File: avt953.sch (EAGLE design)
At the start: 10 parts, among them IC1 AT24CP, IC4 MAX232ECWE, X1 RJ45-6L2-B, X2 MKDS_5/3-7,62

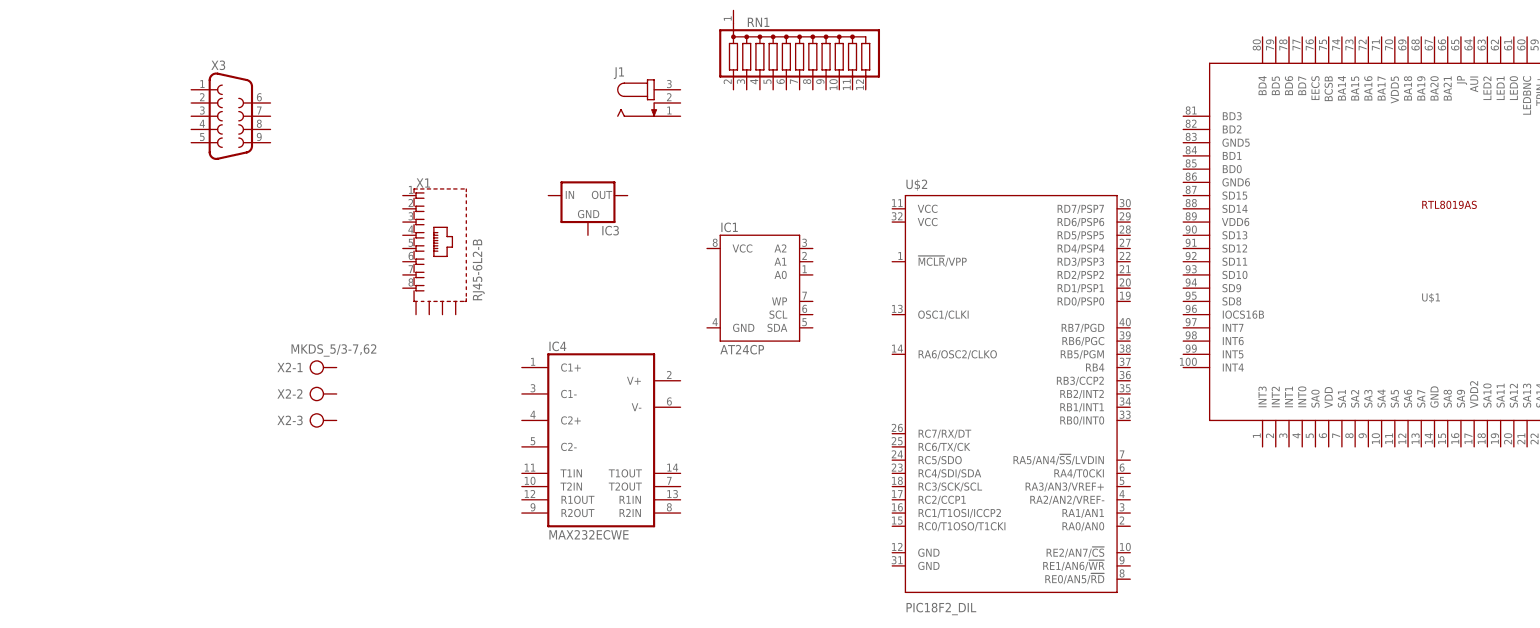
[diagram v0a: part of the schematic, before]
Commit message: Dopasowano nazwy na schemacie do wytycznych.
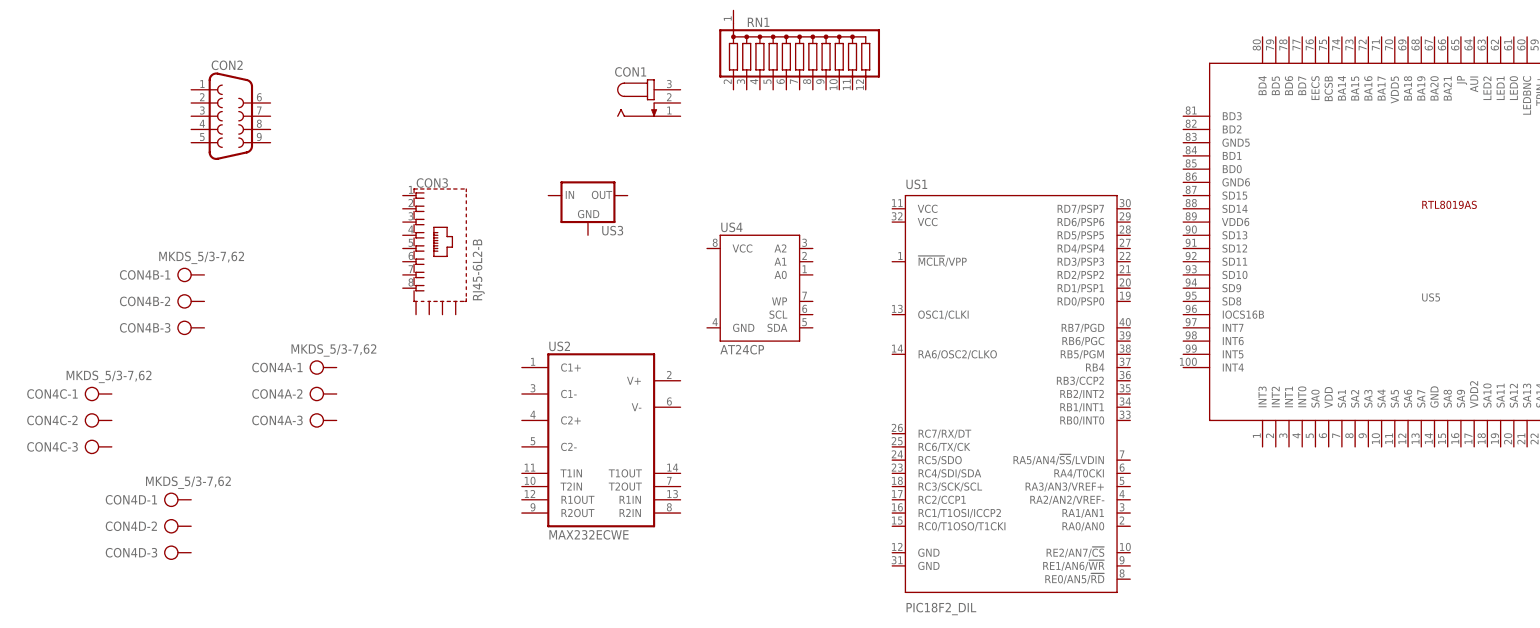
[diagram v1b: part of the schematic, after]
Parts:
- added CON4B, CON4C, CON4D: MKDS_5/3-7,62, con-phoenix-mkds_5:MKDS_5/3-7,62
- renumbered IC1 to US4, IC3 to US3, IC4 to US2, J1 to CON1, U$1 to US5, U$2 to US1, X1 to CON3, X2 to CON4A, X3 to CON2
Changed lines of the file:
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@@
 </classes>
 <parts>
-<part name="X1" library="con-tycoelectronics" deviceset="RJ45*2" device="-B" technology="-6L"/>
-<part name="IC1" library="atmel" deviceset="AT24C*" device="P"/>
-<part name="U$1" library="rtl8019as" deviceset="RTL8019AS" device=""/>
-<part name="IC3" library="v-reg" deviceset="78XXL" device=""/>
-<part name="J1" library="con-jack" deviceset="JACK-PLUG" device="0"/>
-<part name="X2" library="con-phoenix-mkds_5" deviceset="MKDS_5/3-" device="7,62"/>
-<part name="X3" library="con-subd" deviceset="F09" device="HP"/>
-<part name="IC4" library="maxim" deviceset="MAX232ECWE" device=""/>
+<part name="CON3" library="con-tycoelectronics" deviceset="RJ45*2" device="-B" technology="-6L"/>
+<part name="US4" library="atmel" deviceset="AT24C*" device="P"/>
+<part name="US5" library="rtl8019as" deviceset="RTL8019AS" device=""/>
+<part name="US3" library="v-reg" deviceset="78XXL" device=""/>
+<part name="CON1" library="con-jack" deviceset="JACK-PLUG" device="0"/>
+<part name="CON4A" library="con-phoenix-mkds_5" deviceset="MKDS_5/3-" device="7,62"/>
+<part name="CON2" library="con-subd" deviceset="F09" device="HP"/>
+<part name="US2" library="maxim" deviceset="MAX232ECWE" device=""/>
 <part name="RN1" library="resistor-sil" deviceset="G11R" device=""/>
-<part name="U$2" library="microchip-custom" deviceset="PIC18F*2_DIL" device=""/>
+<part name="US1" library="microchip-custom" deviceset="PIC18F*2_DIL" device=""/>
+<part name="CON4B" library="con-phoenix-mkds_5" deviceset="MKDS_5/3-" device="7,62"/>
+<part name="CON4C" library="con-phoenix-mkds_5" deviceset="MKDS_5/3-" device="7,62"/>
+<part name="CON4D" library="con-phoenix-mkds_5" deviceset="MKDS_5/3-" device="7,62"/>
 </parts>
 <sheets>
@@
 </plain>
 <instances>
-<instance part="X1" gate="G$1" x="40.64" y="50.8"/>
-<instance part="IC1" gate="G$1" x="101.6" y="43.18"/>
-<instance part="U$1" gate="G$1" x="233.68" y="50.8"/>
-<instance part="IC3" gate="A" x="68.58" y="60.96"/>
-<instance part="J1" gate="G$1" x="81.28" y="78.74"/>
-<instance part="X2" gate="-1" x="15.24" y="27.94"/>
-<instance part="X2" gate="-2" x="15.24" y="22.86"/>
-<instance part="X2" gate="-3" x="15.24" y="17.78"/>
-<instance part="X3" gate="G$1" x="0" y="76.2"/>
-<instance part="IC4" gate="G$1" x="71.12" y="15.24"/>
+<instance part="CON3" gate="G$1" x="40.64" y="50.8"/>
+<instance part="US4" gate="G$1" x="101.6" y="43.18"/>
+<instance part="US5" gate="G$1" x="233.68" y="50.8"/>
+<instance part="US3" gate="A" x="68.58" y="60.96"/>
+<instance part="CON1" gate="G$1" x="81.28" y="78.74"/>
+<instance part="CON4A" gate="-1" x="15.24" y="27.94"/>
+<instance part="CON4A" gate="-2" x="15.24" y="22.86"/>
+<instance part="CON4A" gate="-3" x="15.24" y="17.78"/>
+<instance part="CON2" gate="G$1" x="0" y="76.2"/>
+<instance part="US2" gate="G$1" x="71.12" y="15.24"/>
 <instance part="RN1" gate="A" x="109.22" y="86.36"/>
-<instance part="U$2" gate="G$1" x="149.86" y="22.86"/>
+<instance part="US1" gate="G$1" x="149.86" y="22.86"/>
+<instance part="CON4B" gate="-1" x="-10.16" y="45.72"/>
+<instance part="CON4B" gate="-2" x="-10.16" y="40.64"/>
+<instance part="CON4B" gate="-3" x="-10.16" y="35.56"/>
+<instance part="CON4C" gate="-1" x="-27.94" y="22.86"/>
+<instance part="CON4C" gate="-2" x="-27.94" y="17.78"/>
+<instance part="CON4C" gate="-3" x="-27.94" y="12.7"/>
+<instance part="CON4D" gate="-1" x="-12.7" y="2.54"/>
+<instance part="CON4D" gate="-2" x="-12.7" y="-2.54"/>
+<instance part="CON4D" gate="-3" x="-12.7" y="-7.62"/>
 </instances>
 <busses>

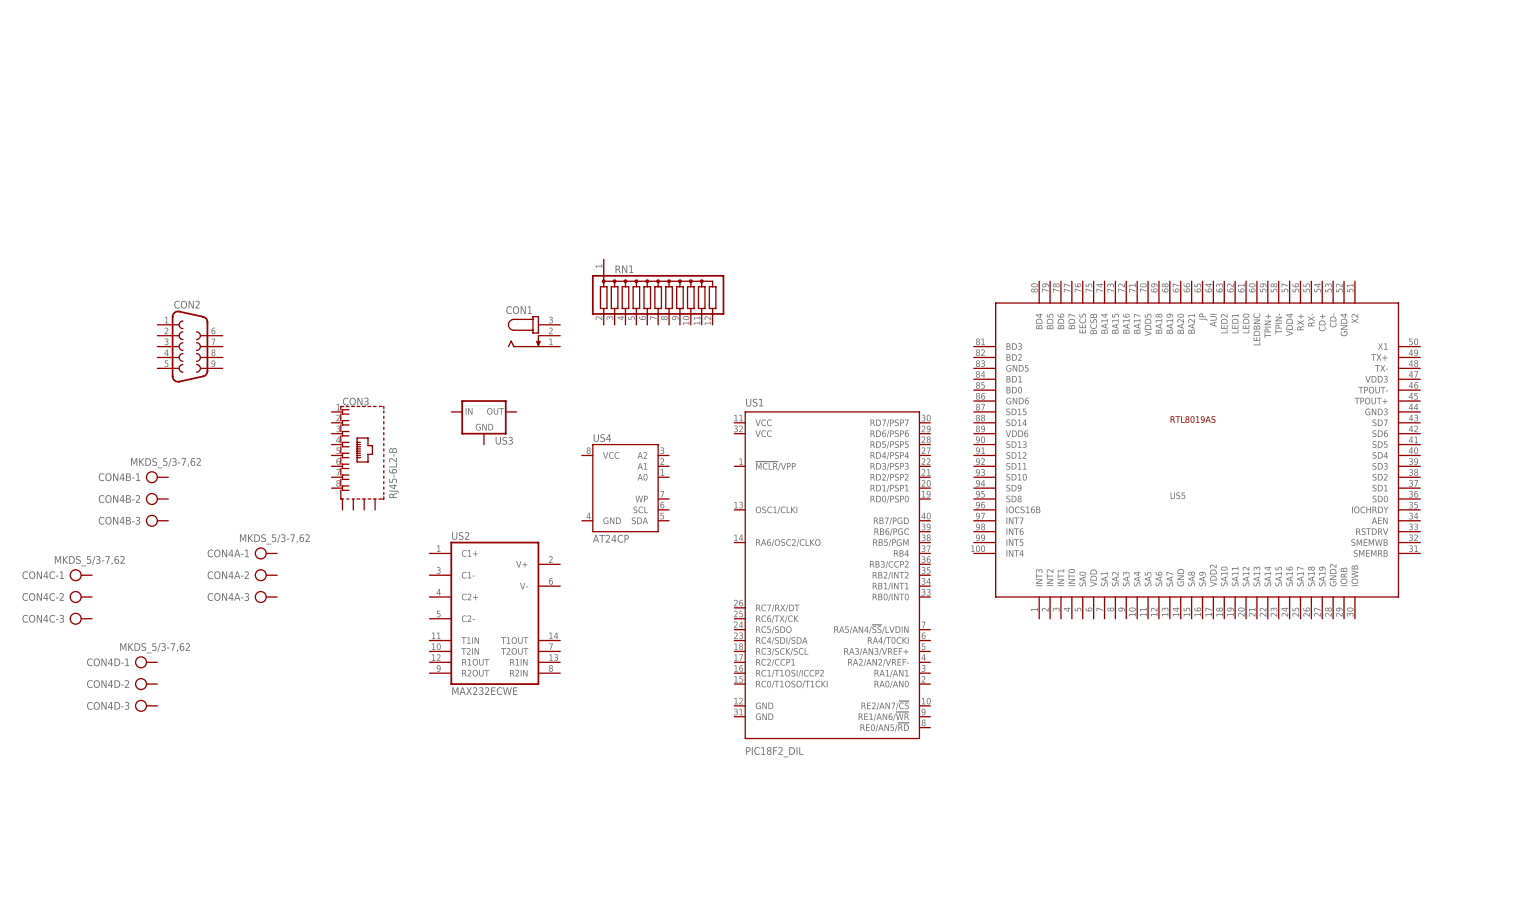
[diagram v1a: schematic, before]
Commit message: Dodano bibliotekę z transformatorem ethernetowym 10BASE-T YCL-20F001N. Umieszczono to trafo na schemacie.
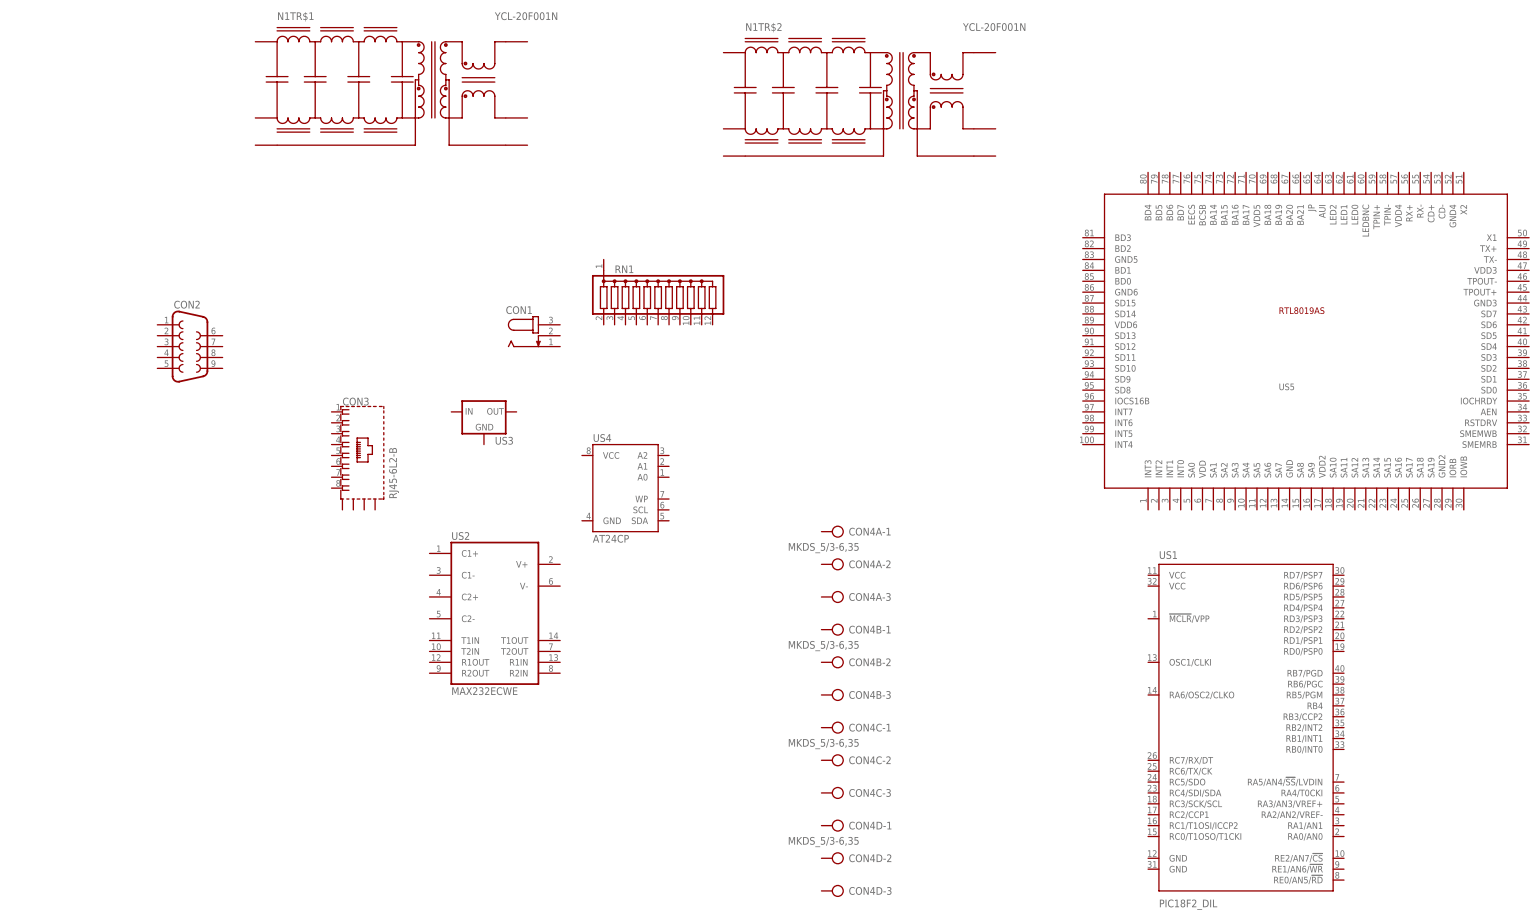
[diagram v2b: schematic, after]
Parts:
- added N1: YCL-20F001N, trafo:YCL-20F001N
- CON4A, CON4B, CON4C, CON4D: value MKDS_5/3-7,62 -> MKDS_5/3-6,35; device con-phoenix-mkds_5:MKDS_5/3-7,62 -> con-phoenix-mkds_5:MKDS_5/3-6,35
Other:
- moved on the sheet: CON4A-1, CON4A-2, CON4A-3, CON4B-1, CON4B-2, CON4B-3, CON4C-1, CON4C-2, CON4C-3, CON4D-1, CON4D-2, CON4D-3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
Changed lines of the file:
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@@
 <part name="US3" library="v-reg" deviceset="78XXL" device=""/>
 <part name="CON1" library="con-jack" deviceset="JACK-PLUG" device="0"/>
-<part name="CON4A" library="con-phoenix-mkds_5" deviceset="MKDS_5/3-" device="7,62"/>
+<part name="CON4A" library="con-phoenix-mkds_5" deviceset="MKDS_5/3-" device="6,35" value="MKDS_5/3-6,35"/>
 <part name="CON2" library="con-subd" deviceset="F09" device="HP"/>
 <part name="US2" library="maxim" deviceset="MAX232ECWE" device=""/>
 <part name="RN1" library="resistor-sil" deviceset="G11R" device=""/>
 <part name="US1" library="microchip-custom" deviceset="PIC18F*2_DIL" device=""/>
-<part name="CON4B" library="con-phoenix-mkds_5" deviceset="MKDS_5/3-" device="7,62"/>
-<part name="CON4C" library="con-phoenix-mkds_5" deviceset="MKDS_5/3-" device="7,62"/>
-<part name="CON4D" library="con-phoenix-mkds_5" deviceset="MKDS_5/3-" device="7,62"/>
+<part name="CON4B" library="con-phoenix-mkds_5" deviceset="MKDS_5/3-" device="6,35" value="MKDS_5/3-6,35"/>
+<part name="CON4C" library="con-phoenix-mkds_5" deviceset="MKDS_5/3-" device="6,35" value="MKDS_5/3-6,35"/>
+<part name="CON4D" library="con-phoenix-mkds_5" deviceset="MKDS_5/3-" device="6,35" value="MKDS_5/3-6,35"/>
+<part name="N1" library="trafo" deviceset="YCL-20F001?" device="N"/>
 </parts>
 <sheets>
@@
 <instance part="CON3" gate="G$1" x="40.64" y="50.8"/>
 <instance part="US4" gate="G$1" x="101.6" y="43.18"/>
-<instance part="US5" gate="G$1" x="233.68" y="50.8"/>
+<instance part="US5" gate="G$1" x="259.08" y="76.2"/>
 <instance part="US3" gate="A" x="68.58" y="60.96"/>
 <instance part="CON1" gate="G$1" x="81.28" y="78.74"/>
-<instance part="CON4A" gate="-1" x="15.24" y="27.94"/>
-<instance part="CON4A" gate="-2" x="15.24" y="22.86"/>
-<instance part="CON4A" gate="-3" x="15.24" y="17.78"/>
+<instance part="CON4A" gate="-1" x="152.4" y="33.02" rot="R180"/>
+<instance part="CON4A" gate="-2" x="152.4" y="25.4" rot="R180"/>
+<instance part="CON4A" gate="-3" x="152.4" y="17.78" rot="R180"/>
 <instance part="CON2" gate="G$1" x="0" y="76.2"/>
 <instance part="US2" gate="G$1" x="71.12" y="15.24"/>
 <instance part="RN1" gate="A" x="109.22" y="86.36"/>
-<instance part="US1" gate="G$1" x="149.86" y="22.86"/>
-<instance part="CON4B" gate="-1" x="-10.16" y="45.72"/>
-<instance part="CON4B" gate="-2" x="-10.16" y="40.64"/>
-<instance part="CON4B" gate="-3" x="-10.16" y="35.56"/>
-<instance part="CON4C" gate="-1" x="-27.94" y="22.86"/>
-<instance part="CON4C" gate="-2" x="-27.94" y="17.78"/>
-<instance part="CON4C" gate="-3" x="-27.94" y="12.7"/>
-<instance part="CON4D" gate="-1" x="-12.7" y="2.54"/>
-<instance part="CON4D" gate="-2" x="-12.7" y="-2.54"/>
-<instance part="CON4D" gate="-3" x="-12.7" y="-7.62"/>
+<instance part="US1" gate="G$1" x="246.38" y="-12.7"/>
+<instance part="CON4B" gate="-1" x="152.4" y="10.16" rot="R180"/>
+<instance part="CON4B" gate="-2" x="152.4" y="2.54" rot="R180"/>
+<instance part="CON4B" gate="-3" x="152.4" y="-5.08" rot="R180"/>
+<instance part="CON4C" gate="-1" x="152.4" y="-12.7" rot="R180"/>
+<instance part="CON4C" gate="-2" x="152.4" y="-20.32" rot="R180"/>
+<instance part="CON4C" gate="-3" x="152.4" y="-27.94" rot="R180"/>
+<instance part="CON4D" gate="-1" x="152.4" y="-35.56" rot="R180"/>
+<instance part="CON4D" gate="-2" x="152.4" y="-43.18" rot="R180"/>
+<instance part="CON4D" gate="-3" x="152.4" y="-50.8" rot="R180"/>
+<instance part="N1" gate="TR$1" x="40.64" y="149.86"/>
+<instance part="N1" gate="TR$2" x="149.86" y="147.32"/>
 </instances>
 <busses>

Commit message: Zaprojektowano kompletny schemat układu.Przygotowano na jego podstawie pusty projekt płytki PCB i rozmieszczono co większe elementy.
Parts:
- removed RN1: (no value), resistor-sil:G11R
- added C1: 100u, resistor:CPOL-EUE5-13
- added C10, C11, C12, C2, C8, C9: 100n, resistor:C-EUC1206K
- added C13, C14, C15, C16, C17, C18, C21, C6, C7: 100N, resistor:C-EUC1206K
- added C19, C20: 100n,400V, resistor:C-EU075-032X103
- added C3: 220u, resistor:CPOL-EUE5-13
- added C4, C5: 15p, resistor:C-EUC1206K
- added D1: 1N4147, diode:1N4148DO35-10
- added D2: SYSTEM, led:LED5MM
- added D3, D5: LL4148, diode:CGRM4001-G
- added LED: TX_RX, led:LED5MM
- added R13: 11x10k, resistor-sil:G11R
- added R2, R9: 330, resistor:R-EU_M3216
- added R3: 10K, resistor:R-EU_M3216
- added R4, R5: 4K7, resistor:R-EU_M3216
- added R6: 20K, resistor:R-EU_M3216
- added R7: 200, resistor:R-EU_M3216
- added R8: 22K, resistor:R-EU_M3216
- added S: (no value), switch-omron:10-XX
- added X1, X2: 20MHz, crystal:CRYSTALHC49S
- US2: value MAX232ECWE -> MAX232A
- US3: value (none) -> 78L08
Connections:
- new net A0: US1.RB0/INT0, US5.SA0
- new net A1: US1.RB1/INT1, US5.SA1
- new net A2: US1.RB2/INT2, US5.SA2
- new net A3: US1.RB3/CCP2, US5.SA3
- new net A4: US1.RB4, US5.SA4
- new net GND: C1.-, C11.2, C12.2, C13.1, C14.2, C15.2, C16.1, C17.2, C18.2, C19.2, C2.2, C20.2, C21.2, C3.-, C4.2, C5.2, C6.2, C7.2, CON1.1, CON1.2, CON3.S@1, CON3.S@2, CON3.S@3, CON3.S@4, CON4D-3.KL, LED.C, R8.1, S.S, S.S1, US1.GND, US1.GND@1, US2G$1.T2IN, US3.GND, US4.A0, US4.A1, US4.A2, US4.GND, US4.WP, US5.AEN, US5.AUI, US5.GND, US5.GND2, US5.GND3, US5.GND4, US5.GND5, US5.GND6, US5.SA10, US5.SA11, US5.SA12, US5.SA13, US5.SA14, US5.SA15, US5.SA16, US5.SA17, US5.SA18, US5.SA19, US5.SA5, US5.SA6, US5.SA7
- new net IN0: CON4A-1.KL, R13.12, US1.RA0/AN0
- new net IN1: CON4A-2.KL, R13.11, US1.RA1/AN1
- new net IN10: CON4D-2.KL, R13.2, US1.RC5/SDO
- new net IN2: CON4A-3.KL, R13.10, US1.RA2/AN2/VREF-
- new net IN3: CON4B-1.KL, R13.9, US1.RA3/AN3/VREF+
- new net IN4: CON4B-2.KL, R13.8, US1.RA5/AN4/!SS!/LVDIN
- new net IN5: CON4B-3.KL, R13.7, US1.RB6/PGC
- new net IN6: CON4C-1.KL, R13.6, US1.RB7/PGD
- new net IN7: CON4C-2.KL, R13.5, US1.RC0/T1OSO/T1CKI
- new net IN8: CON4C-3.KL, R13.4, US1.RC1/T1OSI/ICCP2
- new net IN9: CON4D-1.KL, R13.3, US1.RC2/CCP1
- new net IOR: US1.RE0/AN5/!RD, US5.IORB
- new net IOW: US1.RE1/AN6/!WR, US5.IOWB
- new net N$1: C9.2, US2G$1.V+
- new net N$10: CON2.7, US2G$1.R2IN
- new net N$11: CON1.3, D1.A
- new net N$12: C1.+, D1.C, US3.IN
- new net N$13: CON3.1, N1TR$1.P$4
- new net N$14: CON3.2, N1TR$1.P$6
- new net N$15: CON3.3, N1TR$2.P$4
- new net N$16: CON3.6, N1TR$2.P$6
- new net N$17: C19.1, N1TR$1.P$5
- new net N$18: C20.1, N1TR$2.P$5
- new net N$19: C18.1, N1TR$2.P$2
- new net N$2: C12.1, US2G$1.V-
- new net N$20: C17.1, N1TR$1.P$2
- new net N$21: N1TR$1.P$3, US5.TPOUT+
- new net N$22: N1TR$2.P$3, R7.1, US5.TPIN+
- new net N$23: N1TR$1.P$1, US5.TPOUT-
- new net N$24: US5.X1, X2.2
- new net N$25: N1TR$2.P$1, R7.2, US5.TPIN-
- new net N$26: D3.A, US5.LED1
- new net N$27: R8.2, US5.IOCS16B
- new net N$28: US5.X2, X2.1
- new net N$29: D5.A, US5.LED2
- new net N$3: C10.2, US2G$1.C1-
- new net N$30: D3.C, D5.C, R9.2
- new net N$31: LED.A, R9.1
- new net N$32: C5.1, US1.OSC1/CLKI, X1.1
- new net N$33: C4.1, US1.RA6/OSC2/CLKO, X1.2
- new net N$34: R4.2, US1.RC4/SDI/SDA, US4.SDA
- new net N$35: R3.1, US1.!MCLR!/VPP
- new net N$36: R2.2, US1.RA4/T0CKI
- new net N$37: R5.2, US1.RC3/SCK/SCL, US4.SCL
- new net N$38: D2.C, R2.1
- new net N$4: C10.1, US2G$1.C1+
- new net N$40: S.P, S.P1, US1.RB5/PGM
- new net N$5: C8.1, US2G$1.C2+
- new net N$6: C8.2, US2G$1.C2-
- new net N$7: CON2.2, US2G$1.T1OUT
- new net N$8: CON2.8, US2G$1.T2OUT
- new net N$9: CON2.3, US2G$1.R1IN
- new net RESET: R6.1, US1.RE2/AN7/!CS, US5.RSTDRV
- new net RXD: US1.RC7/RX/DT, US2G$1.R1OUT
- new net SD0: US1.RD0/PSP0, US5.SD0
- new net SD1: US1.RD1/PSP1, US5.SD1
- new net SD2: US1.RD2/PSP2, US5.SD2
- new net SD3: US1.RD3/PSP3, US5.SD3
- new net SD4: US1.RD4/PSP4, US5.SD4
- new net SD5: US1.RD5/PSP5, US5.SD5
- new net SD6: US1.RD6/PSP6, US5.SD6
- new net SD7: US1.RD7/PSP7, US5.SD7
- new net TXD: US1.RC6/TX/CK, US2G$1.T1IN
- new net VCC: C11.1, C13.2, C14.1, C15.1, C16.2, C2.1, C21.1, C3.+, C6.1, C7.1, C9.1, D2.A, R13.1, R3.2, R4.1, R5.1, R6.2, US1.VCC, US1.VCC@1, US3.OUT, US4.VCC, US5.SA8, US5.SA9, US5.SMEMRB, US5.SMEMWB, US5.VDD, US5.VDD2, US5.VDD4, US5.VDD5, US5.VDD6
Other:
- moved on the sheet: CON1, CON2, CON3, CON4A-1, CON4A-2, CON4A-3, CON4B-1, CON4B-2, CON4B-3, CON4C-1, CON4C-2, CON4C-3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
